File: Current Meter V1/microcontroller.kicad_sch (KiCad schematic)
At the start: 1 part

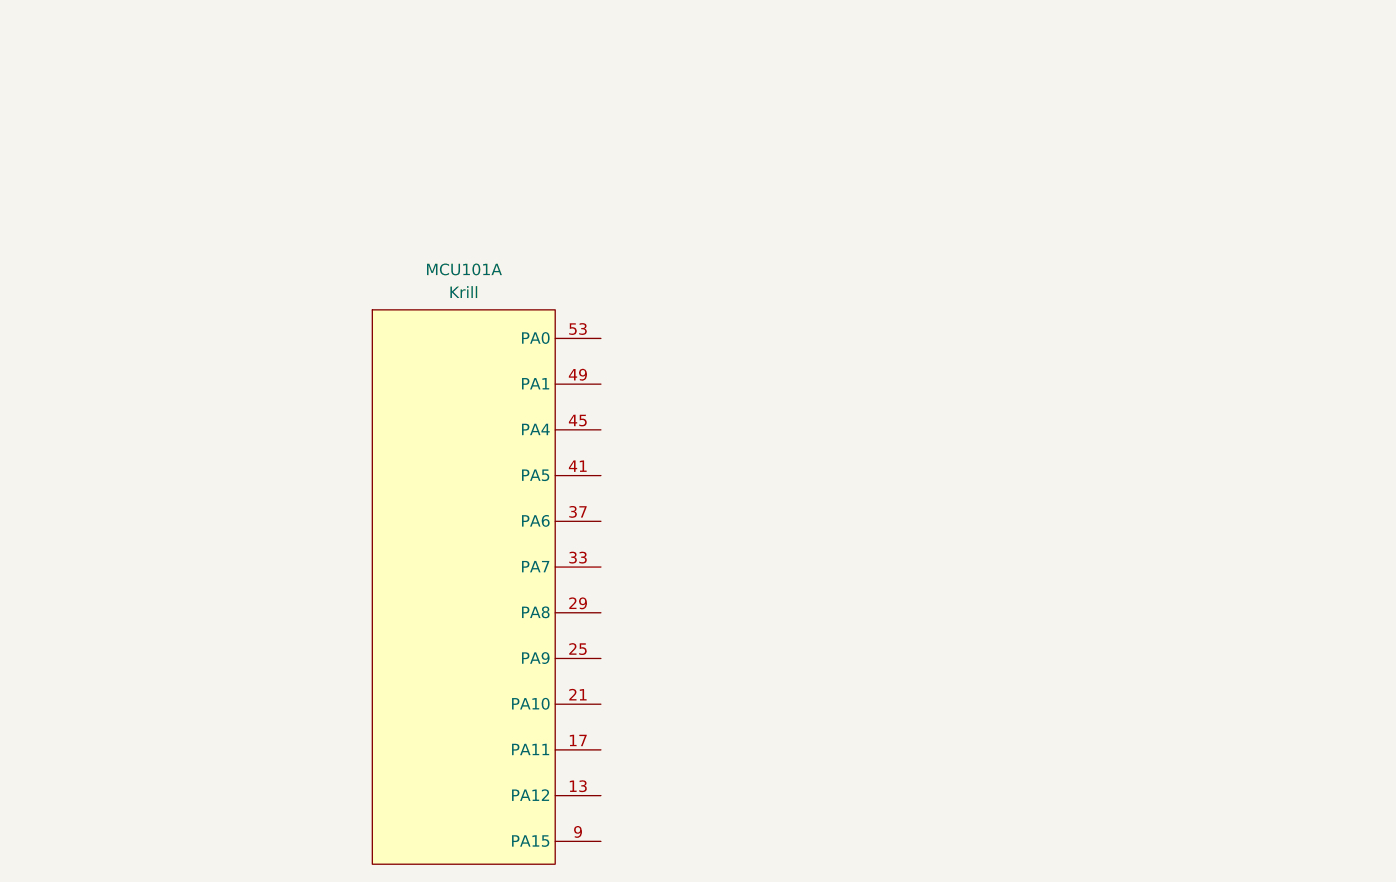
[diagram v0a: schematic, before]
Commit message: Redesign op amp circuit for 0-3.3v output previous design clipped to negative
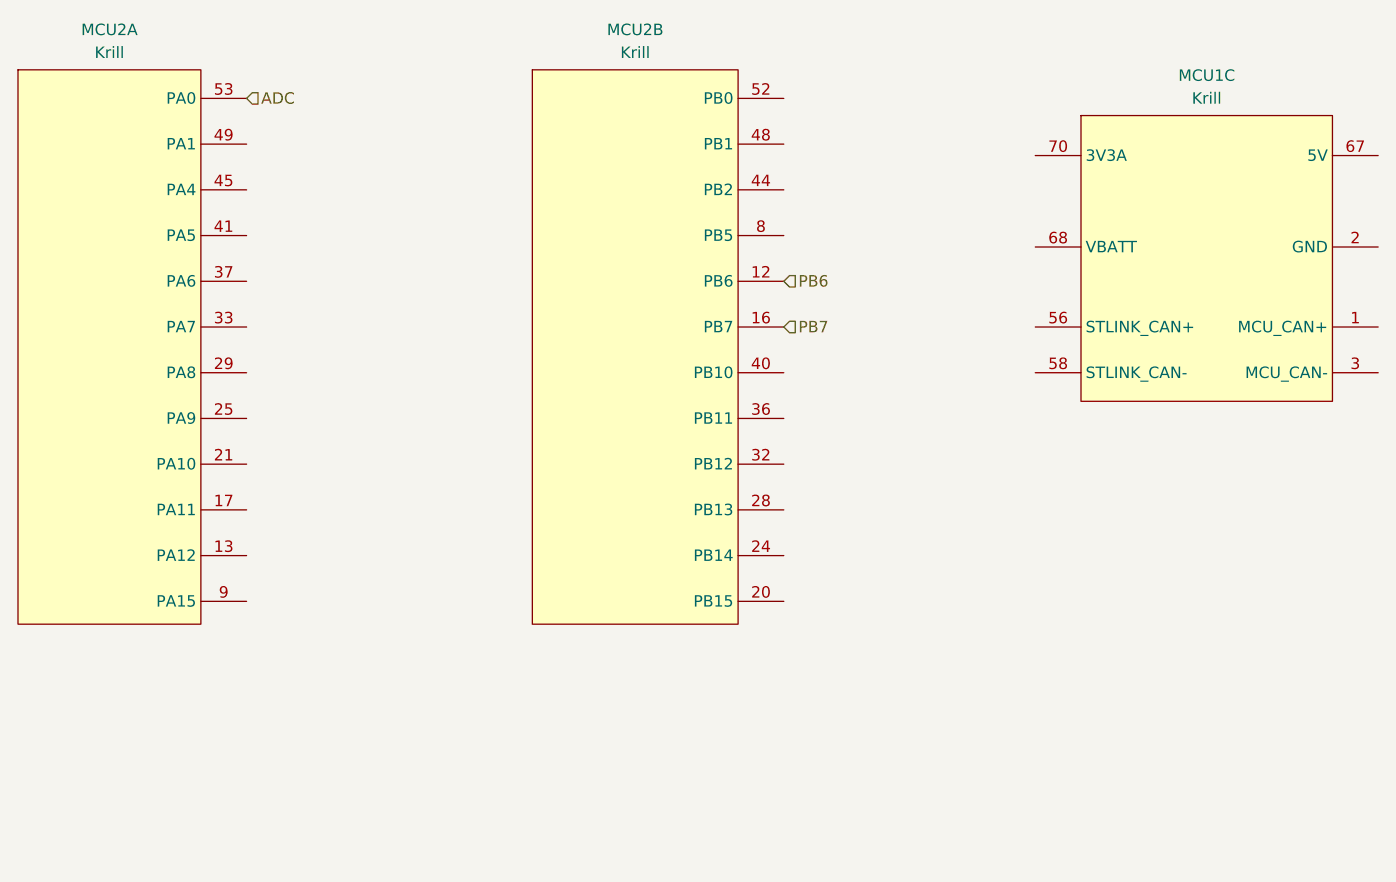
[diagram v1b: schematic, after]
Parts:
- removed MCU101: Krill, bfr_connectors:TE_1-2199119-5, symbol bfr_microcontrollers:Krill
- added MCU1, MCU2: Krill, bfr_connectors:TE_1-2199119-5, symbol bfr_microcontrollers:Krill
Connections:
- new net: MCU1.10 (GND), MCU1.11 (GND), MCU1.14 (GND), MCU1.15 (GND), MCU1.18 (GND), MCU1.19 (GND), MCU1.2 (GND), MCU1.22 (GND), MCU1.23 (GND), MCU1.26 (GND), MCU1.27 (GND), MCU1.30 (GND), MCU1.31 (GND), MCU1.34 (GND), MCU1.35 (GND), MCU1.38 (GND), MCU1.39 (GND), MCU1.4 (GND), MCU1.42 (GND), MCU1.43 (GND), MCU1.46 (GND), MCU1.47 (GND), MCU1.5 (GND), MCU1.50 (GND), MCU1.51 (GND), MCU1.54 (GND), MCU1.55 (GND), MCU1.57 (GND), MCU1.6 (GND), MCU1.7 (GND), MCU1.73 (GND), MCU1.75 (GND)
- new net: MCU1.67 (5V), MCU1.69 (5V), MCU1.71 (5V)
- new net: MCU1.70 (3V3A), MCU1.72 (3V3A), MCU1.74 (3V3A)
- new net ADC: MCU2.53 (PA0)
- new net PB6: MCU2.12 (PB6)
- new net PB7: MCU2.16 (PB7)
